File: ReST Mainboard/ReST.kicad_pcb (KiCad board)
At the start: 2 copper layers, 100 x 100 mm, 103 parts, among them IC1 AT24C128, P1 CONN_02X08, P10 CONN_01X04, P11 CONN_01X04, P12 CONN_02X04, P13 CONN_01X03, P14 CONN_02X03, P15 CONN_01X05, P16 CONN_01X03, P17 CONN_01X04, P18 CONN_02X04, P19 CONN_01X04, P2 CONN_02X08, P20 CONN_02X04, P21 CONN_02X04, P22 CONN_01X03, P23 SCREW_01X03, P24 CONN_01X03, P25 SCREW_01X03, P26 CONN_01X03, P27 SCREW_01X03, P28 CONN_01X03, P29 SCREW_01X03, P3 CONN_02X07, P30 CONN_01X03, P31 SCREW_01X03, P32 CONN_01X03, P33 SCREW_01X03, P34 CONN_01X03, P35 SCREW_01X04, P36 SCREW_01X04, P37 SCREW_01X04, P38 SCREW_01X04, P39 CONN_02X04, P4 CONN_02X10, P40 CONN_01X04, P41 CONN_01X04, P42 CONN_01X04, P43 CONN_02X03, P44 CONN_02X03, P45 CONN_02X03, P46 CONN_02X03, P5 USB_OTG, P6 CONN_02X05, P7 CONN_02X05, P8 CONN_01X09, P9 CONN_01X02, SW1 SW-SPST-NO, U1 STM32F103VE, U2 USBLC6-2, U3 L7805ACD2T-TR, U4 LM2574N-ADJ, U5 POLOLU_A4988, U6 POLOLU_A4988, U7 POLOLU_A4988, U8 POLOLU_A4988, X1 8MHZ RESONATOR

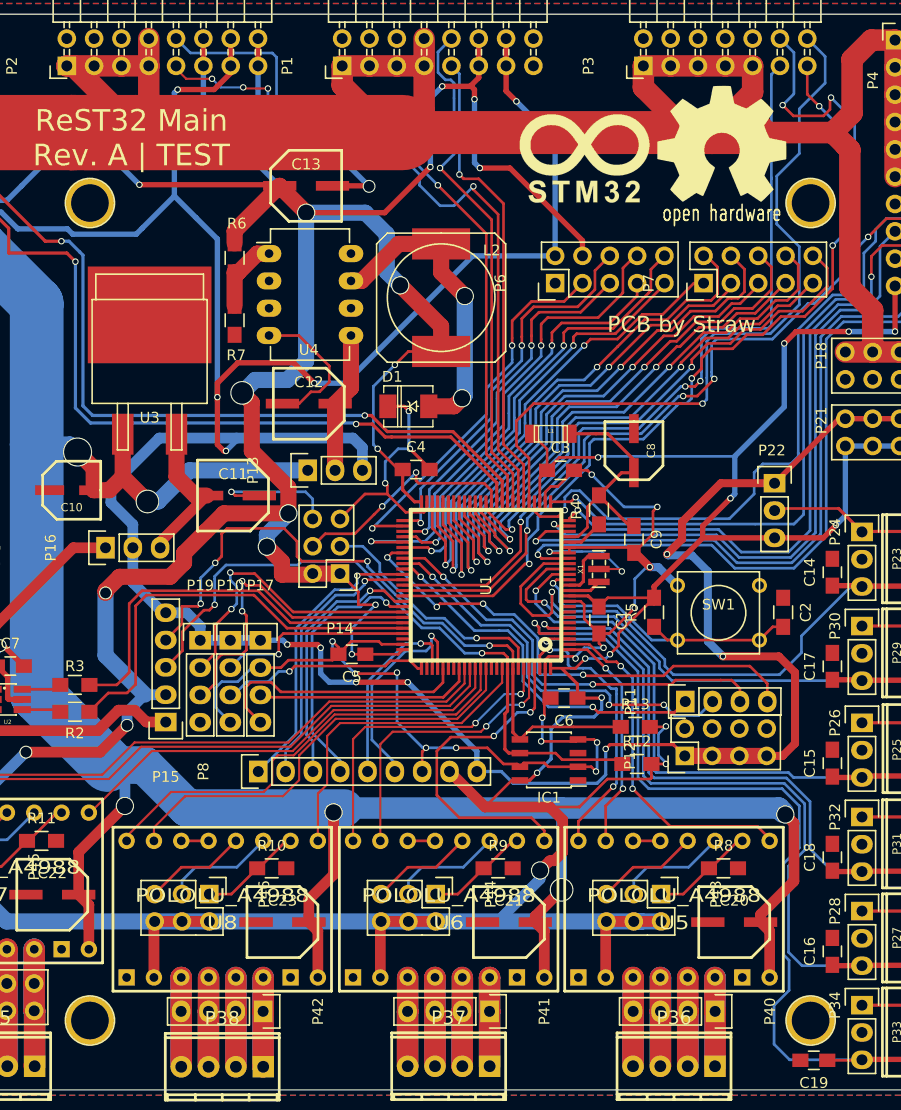
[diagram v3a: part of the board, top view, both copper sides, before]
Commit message: Added BOM and changed Oscillator to Crystal
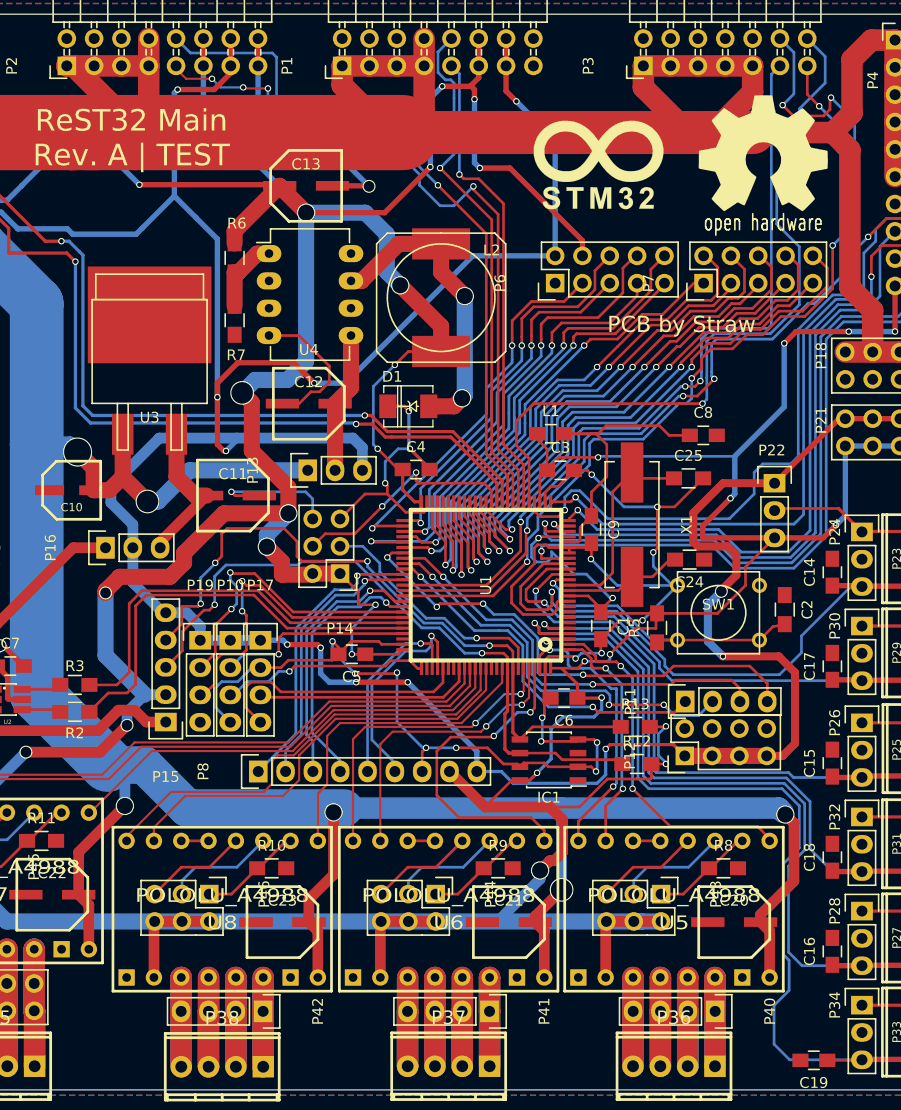
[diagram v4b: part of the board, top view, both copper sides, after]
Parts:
- removed ? (x4): , Connect:1pin
- removed ?: , ReST-Library:Logo_silk_OSHW_12x13mm
- removed R4: 47R, Resistors_SMD:R_0805_HandSoldering
- added C24: 30pF, Resistors_SMD:R_0805_HandSoldering, F.Cu at (175.8, 106.2)
- added C25: 30pF, Resistors_SMD:R_0805_HandSoldering, F.Cu at (175.7, 98.6)
- added G***: LOGO, ReST-Library:Logo_silk_OSHW_12x13mm, F.Cu at (182.6, 68.4)
- C8: footprint ok-polcaps-panasonic:CP-PANASONIC-SMT_C -> Capacitors_SMD:C_0805_HandSoldering
- C9: value 10nF -> 100nF
- L1: footprint ok-smd-generic:1206 -> Capacitors_SMD:C_0805_HandSoldering
- X1: value 8MHZ RESONATOR -> Crystal_Small; footprint ReST-Library:SMD-3P -> Crystals:Crystal_HC49-SD_SMD
- moved C8 6.61 mm to (177.0, 94.6), turned to 0 degrees
- moved X1 5.15 mm to (170.4, 102.9), turned to 270 degrees
- moved C9 4.06 mm to (166.6, 103.3)
- moved R5 1.48 mm to (172.7, 112.5)
- moved G*** 1.43 mm to (167.3, 69.6)
- moved C1 0.55 mm to (167.5, 112.3)
- moved C2 0.29 mm to (184.6, 110.8)
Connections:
- C8 pad 1: VREF -> Net-(C8-Pad1)
- C9 pad 1: VREF -> Net-(C8-Pad1)
- L1 pad 2: VREF -> Net-(C8-Pad1)
- U1 pad 12: Net-(U1-Pad12) -> Net-(C24-Pad2)
- U1 pad 13: Net-(U1-Pad13) -> Net-(C25-Pad1)
- U1 pad 21: Net-(R4-Pad1) -> Net-(C8-Pad1)
- U1 pad 22: VREF -> +3V3
- X1 pad 1: Net-(U1-Pad12) -> Net-(C25-Pad1)
- X1 pad 2: Net-(U1-Pad13) -> Net-(C24-Pad2)
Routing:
- net +3V3: track 626.7 -> 651.8 mm, vias 31 -> 33
- net Net-(C8-Pad1): track 0.00 -> 24.2 mm
- net VREF: track 22.2 -> 0.00 mm
- net Net-(C25-Pad1): track 0.00 -> 20.7 mm
- net Net-(C24-Pad2): track 0.00 -> 11.0 mm
- net GND: track 248.3 -> 258.0 mm, vias 25 -> 24
- net Net-(U1-Pad13): track 4.98 -> 0.00 mm
- net Net-(R4-Pad1): track 3.43 -> 0.00 mm
- net Net-(U1-Pad12): track 3.08 -> 0.00 mm
- net /X-MIN: track 57.4 -> 56.6 mm
- net Net-(C2-Pad2): track 29.1 -> 28.6 mm

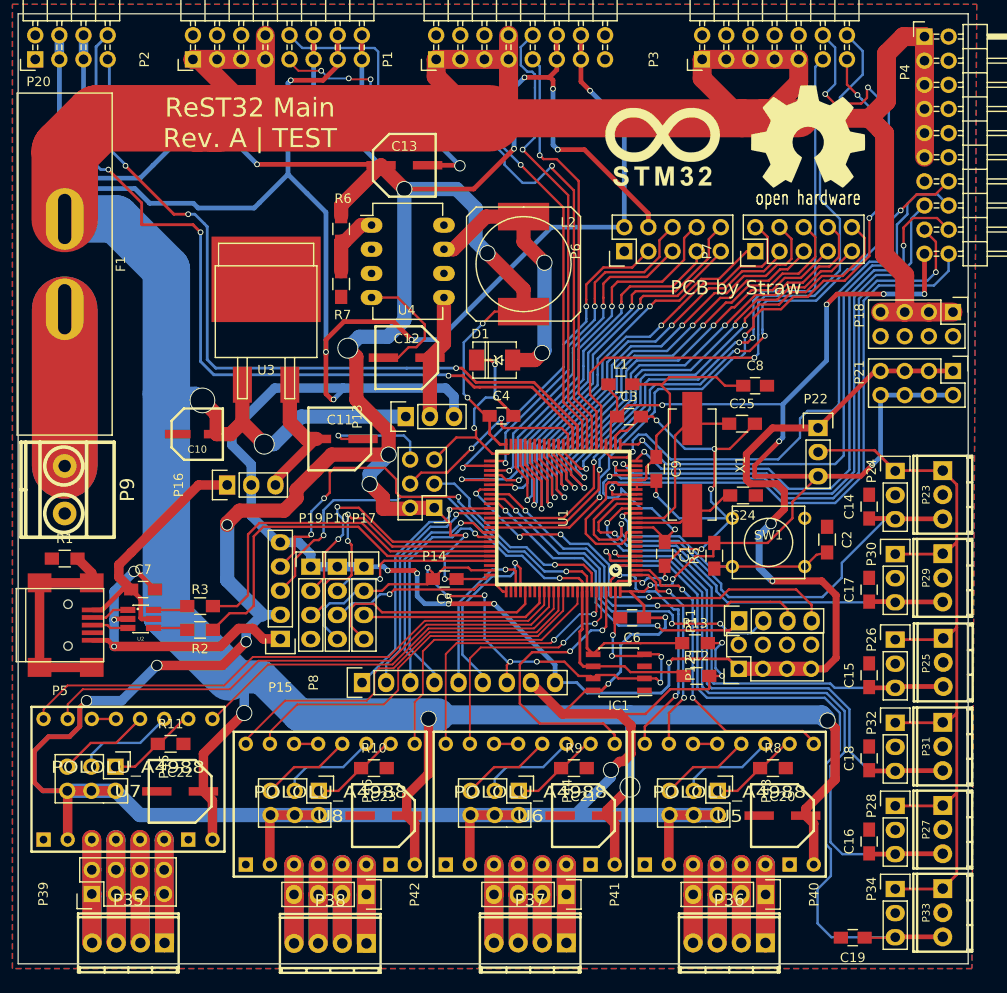
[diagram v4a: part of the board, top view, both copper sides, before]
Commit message: Added Missing Screw Holes on main
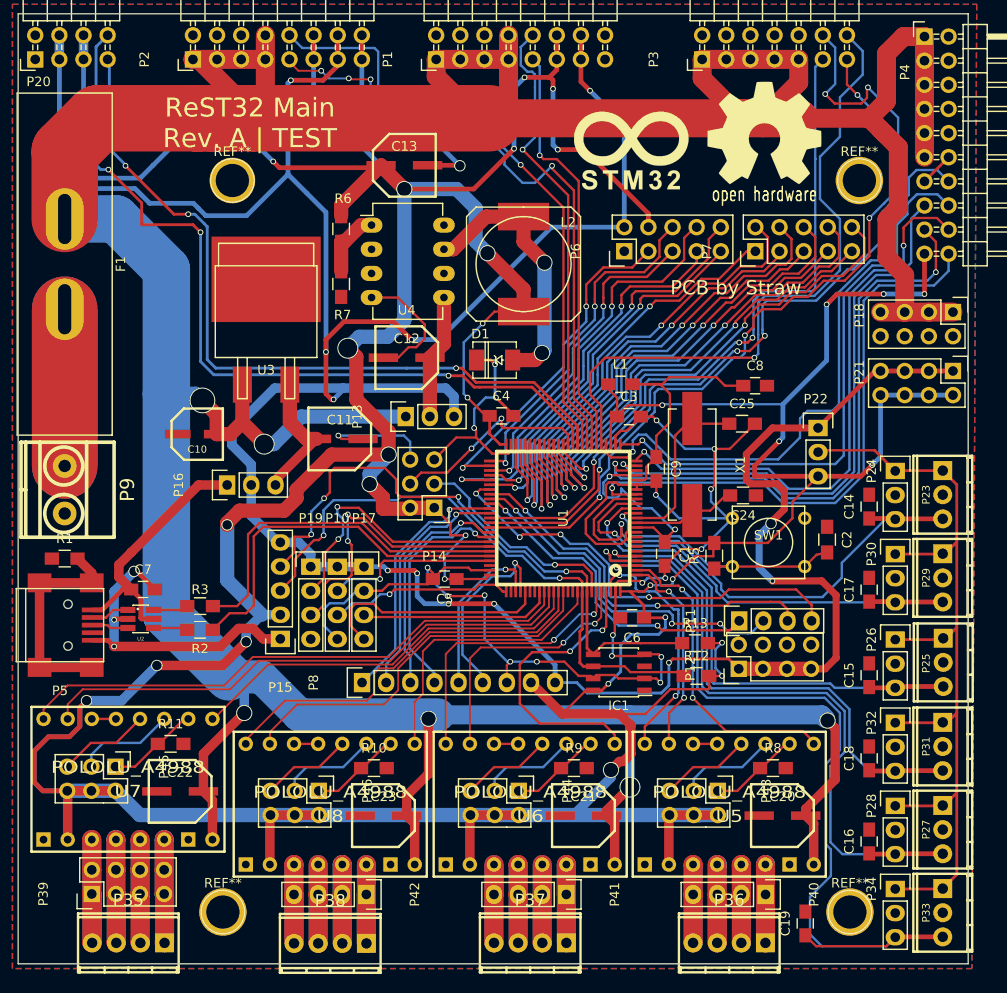
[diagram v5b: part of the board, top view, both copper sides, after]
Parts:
- added REF**: 1pin, Connect:1pin, F.Cu at (188.0, 73.0)
- added REF**: 1pin, Connect:1pin, F.Cu at (122.0, 73.0)
- added REF**: 1pin, Connect:1pin, F.Cu at (121.0, 150.0)
- added REF**: 1pin, Connect:1pin, F.Cu at (187.0, 150.0)
- moved C19 5.22 mm to (182.3, 151.2), turned to 90 degrees
- moved G*** 4.62 mm to (178.0, 68.0)
- moved G*** 3.32 mm to (164.0, 70.0)
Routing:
- net /Z-MAX: track 78.6 -> 88.6 mm
- net GND: track 258.0 -> 261.6 mm
- net /E2-EN: track 62.5 -> 64.7 mm, vias 2 -> 1
- net +12V: track 472.4 -> 473.4 mm
- net +3V3: track 651.8 -> 652.6 mm
- net /PWM-ADD2: track 89.5 -> 90.4 mm
- net /PWM-ADD1: track 79.5 -> 80.2 mm
- net +5V: track 320.0 -> 320.6 mm
